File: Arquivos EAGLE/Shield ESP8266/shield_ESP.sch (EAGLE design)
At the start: 13 parts

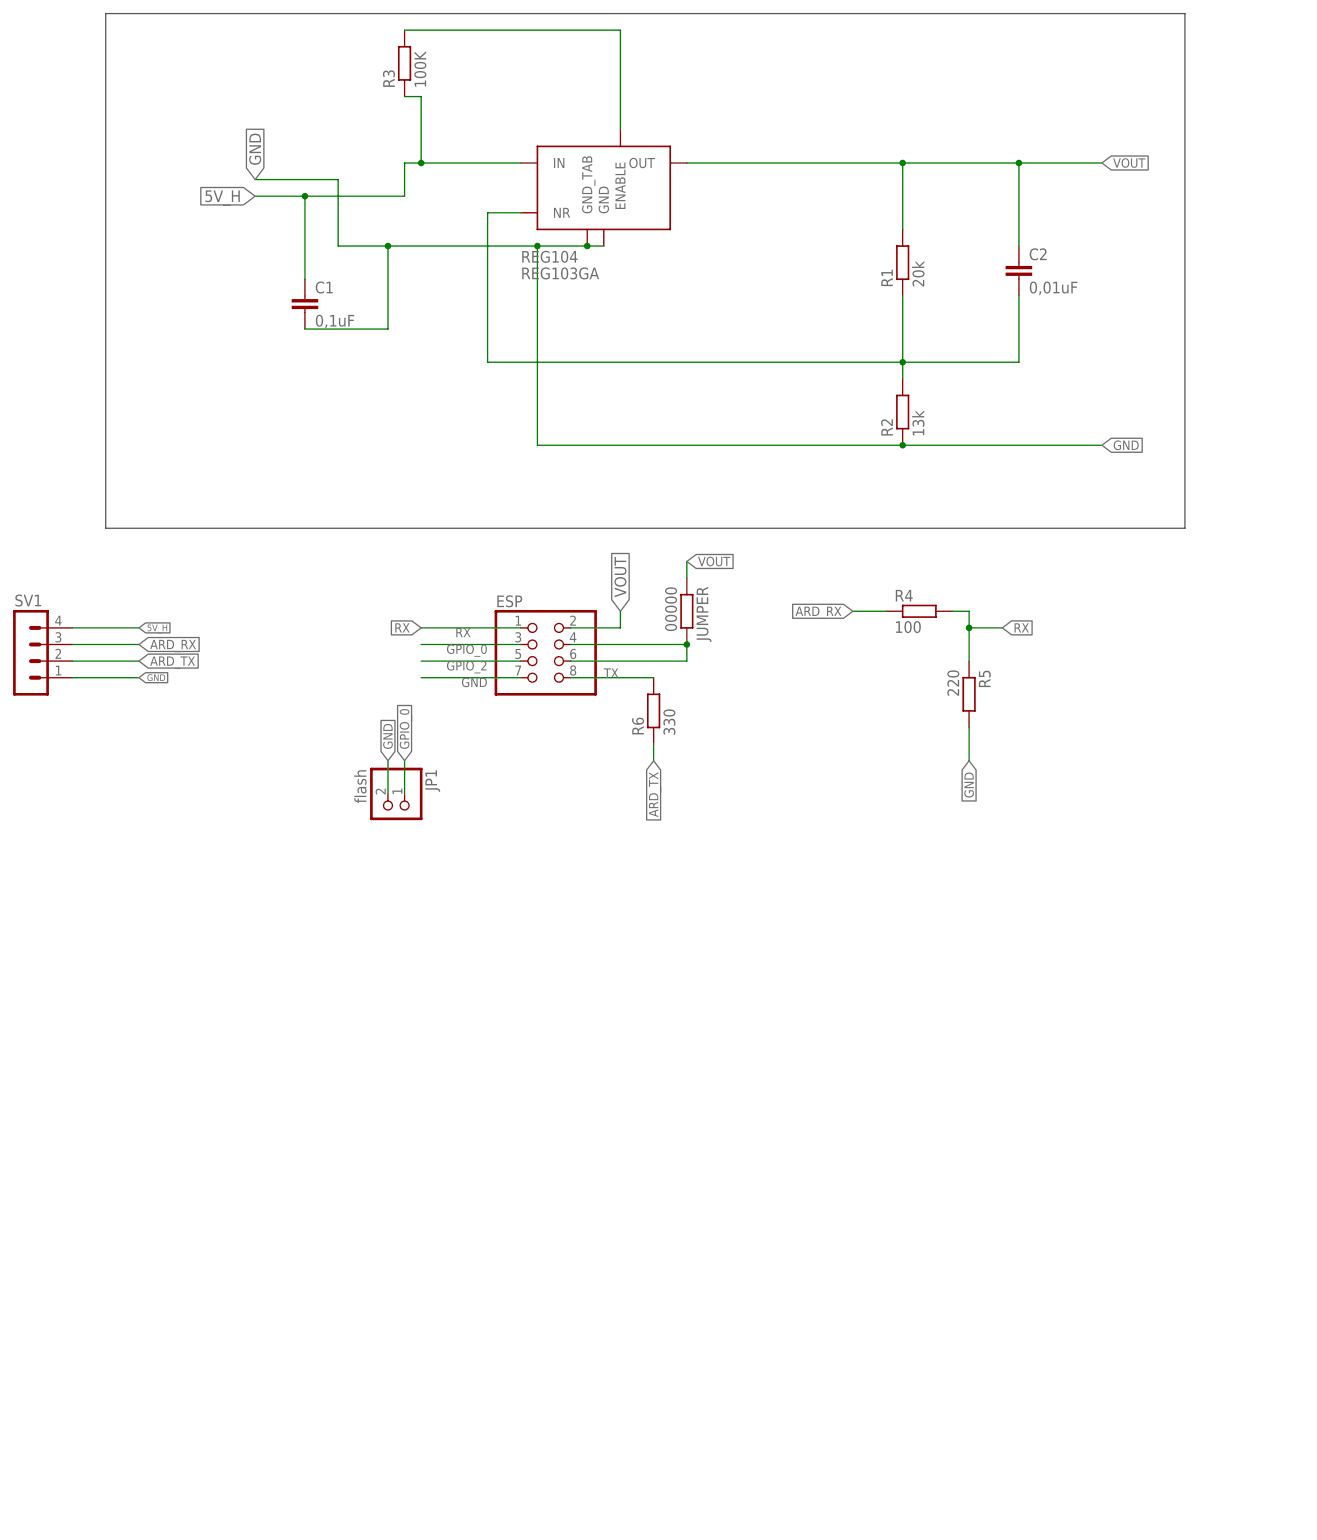
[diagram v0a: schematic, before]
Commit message: Changes in Eagle boards and Arduino libraries
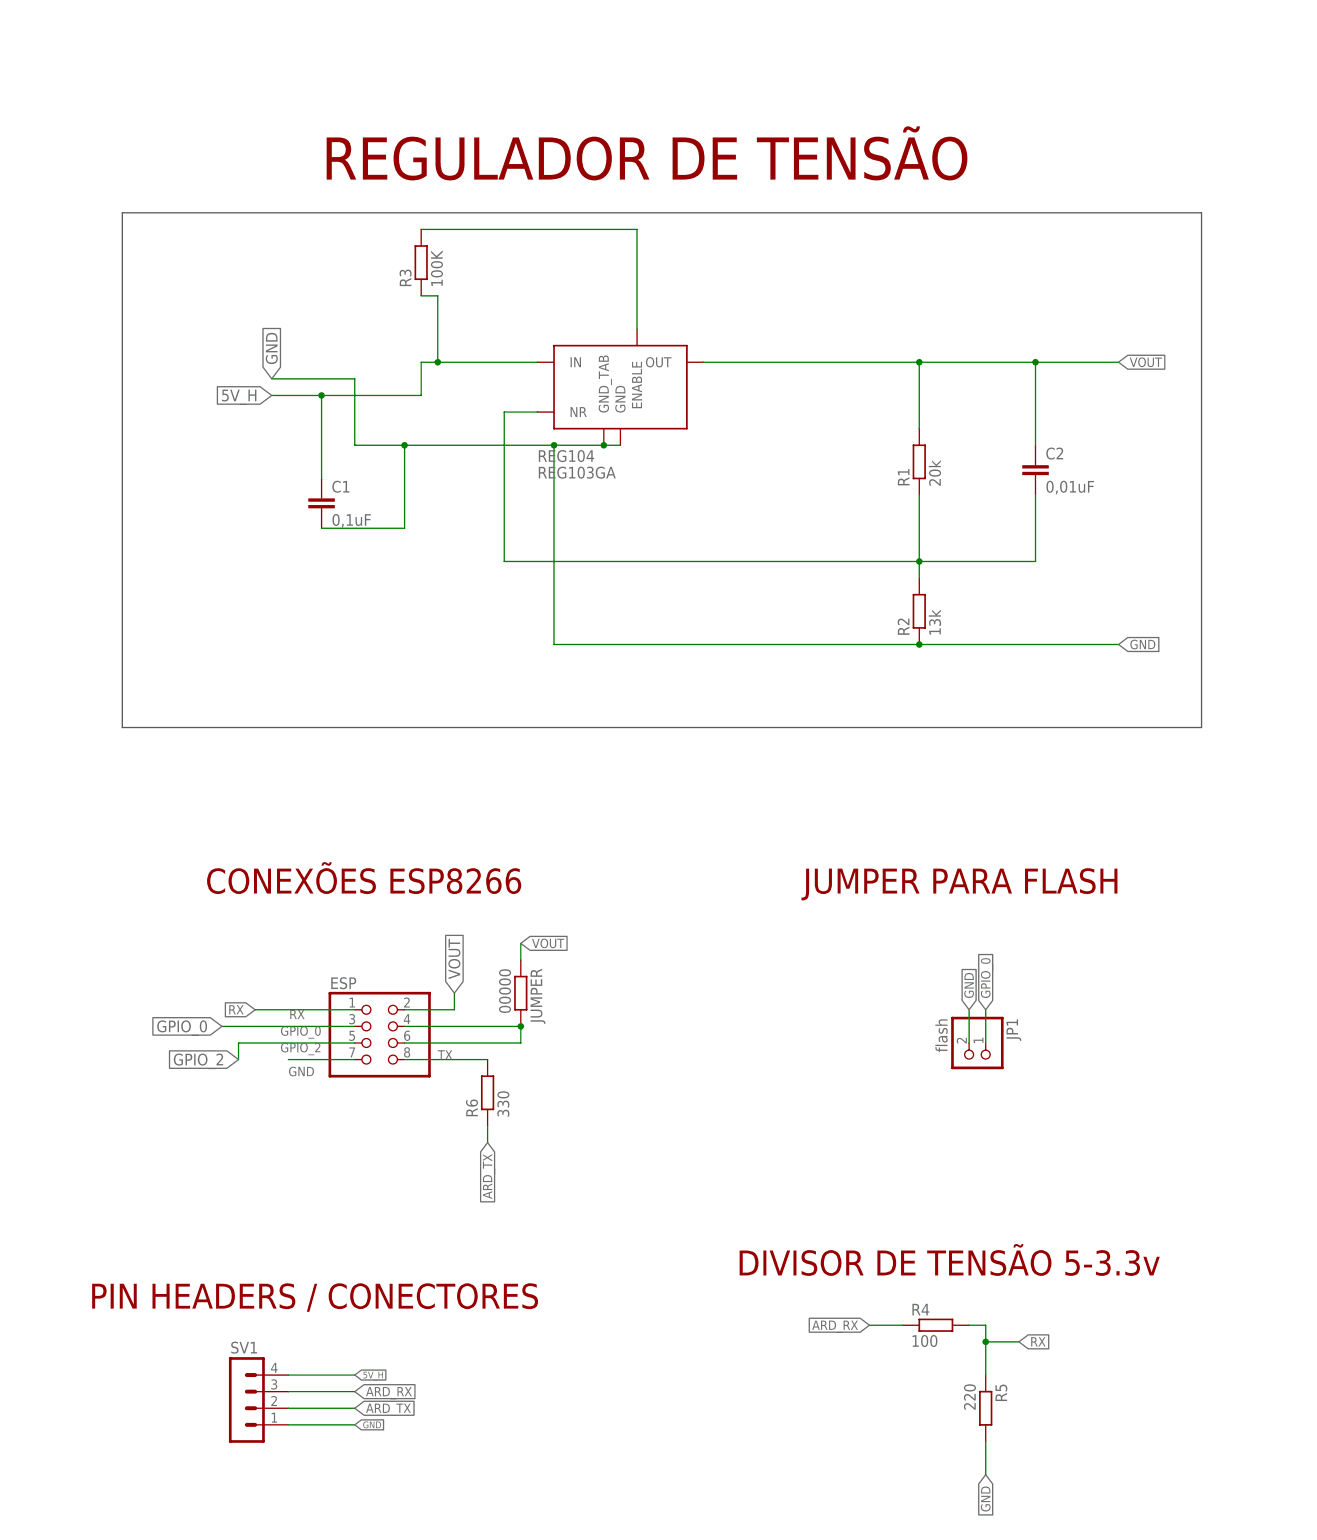
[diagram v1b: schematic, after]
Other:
- note added: "CONEXÕES ESP8266"
- note added: "DIVISOR DE TENSÃO 5-3.3v"
- note added: "JUMPER PARA FLASH"
- note added: "PIN HEADERS / CONECTORES"
- note added: "REGULADOR DE TENSÃO"
- moved on the sheet: C1, C2, ESP, JP1, JUMPER, R1, R2, R3, R4, R5, R6, REG104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
